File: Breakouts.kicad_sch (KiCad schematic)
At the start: 21 parts, among them J1 Conn_01x08, J10 AudioJack3_Switch, J11 Conn_01x03, J12 Conn_01x03, J13 Barrel_Jack_Switch, J14 Conn_01x03, J15 Conn_01x08, J16 Conn_01x08, J2 Conn_01x08, J3 Conn_01x08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

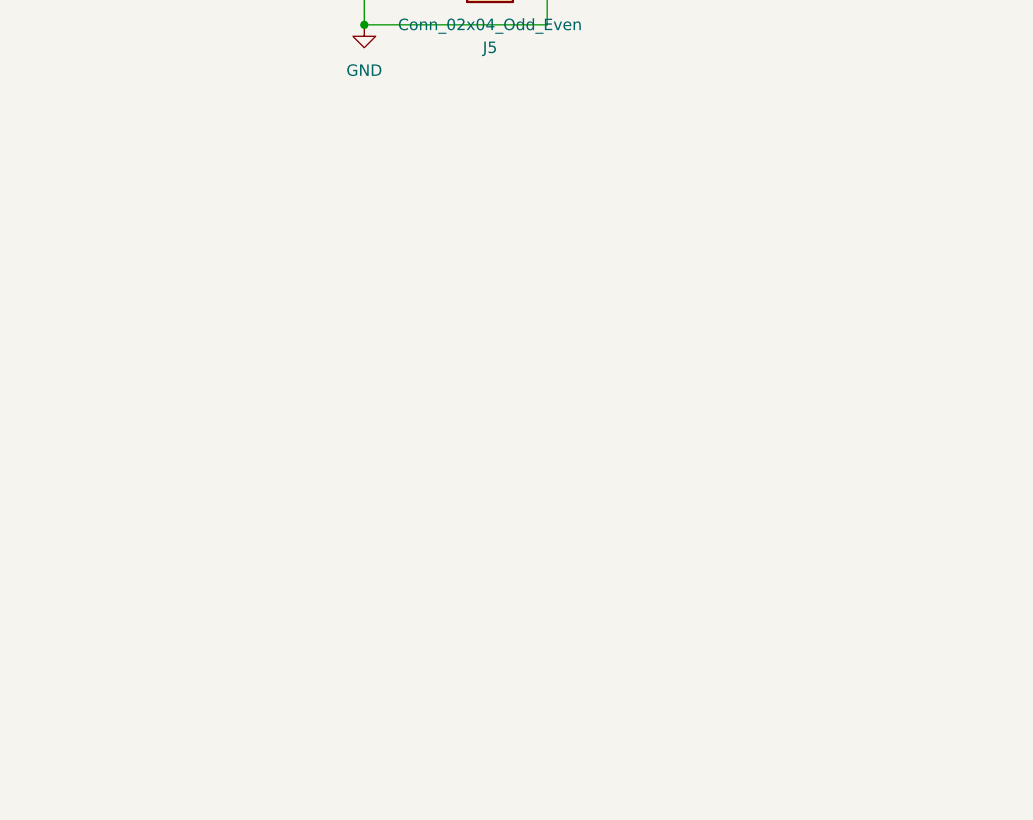
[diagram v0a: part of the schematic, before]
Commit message: Add TDA7575B Breakout
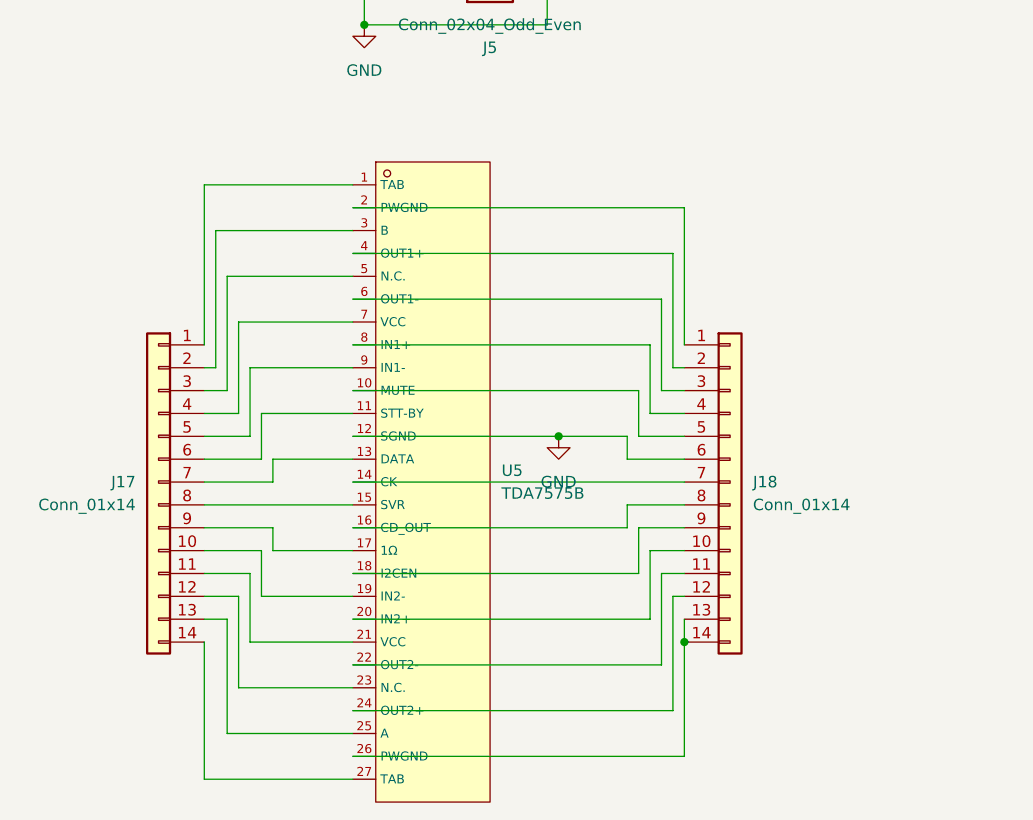
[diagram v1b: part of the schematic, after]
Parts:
- added J17, J18: Conn_01x14, Connector_PinHeader_2.54mm:PinHeader_1x14_P2.54mm_Vertical, symbol Connector_Generic:Conn_01x14
- added U5: TDA7575B, jlc_footprints:FLEXIWATT27-TH_27P-L29.3-W4.6-P1.00, symbol jlc_symbols:TDA7575B
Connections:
- net GND: now also J18.6 (Pin_6), U5.12 (SGND)
- new net: J17.1 (Pin_1), U5.1 (TAB)
- new net: J18.5 (Pin_5), U5.10 (MUTE)
- new net: J17.6 (Pin_6), U5.11 (STT-BY)
- new net: J17.7 (Pin_7), U5.13 (DATA)
- new net: J18.7 (Pin_7), U5.14 (CK)
- new net: J17.8 (Pin_8), U5.15 (SVR)
- new net: J18.8 (Pin_8), U5.16 (CD_OUT)
- new net: J17.9 (Pin_9), U5.17 (1Ω)
- new net: J18.9 (Pin_9), U5.18 (I2CEN)
- new net: J17.10 (Pin_10), U5.19 (IN2-)
- new net: J18.1 (Pin_1), U5.2 (PWGND)
- new net: J18.10 (Pin_10), U5.20 (IN2+)
- new net: J17.11 (Pin_11), U5.21 (VCC)
- new net: J18.11 (Pin_11), U5.22 (OUT2-)
- new net: J17.12 (Pin_12), U5.23 (N.C.)
- new net: J18.12 (Pin_12), U5.24 (OUT2+)
- new net: J17.13 (Pin_13), U5.25 (A)
- new net: J18.13 (Pin_13), J18.14 (Pin_14), U5.26 (PWGND)
- new net: J17.14 (Pin_14), U5.27 (TAB)
- new net: J17.2 (Pin_2), U5.3 (B)
- new net: J18.2 (Pin_2), U5.4 (OUT1+)
- new net: J17.3 (Pin_3), U5.5 (N.C.)
- new net: J18.3 (Pin_3), U5.6 (OUT1-)
- new net: J17.4 (Pin_4), U5.7 (VCC)
- new net: J18.4 (Pin_4), U5.8 (IN1+)
- new net: J17.5 (Pin_5), U5.9 (IN1-)
